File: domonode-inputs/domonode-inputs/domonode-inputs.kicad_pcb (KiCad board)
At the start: 2 copper layers, 95 x 80 mm, 66 parts, among them P1 CONN_01X02, P10 CONN_01X02, P11 CONN_01X02, P12 CONN_02X03, P13 CONN_02X05, P14 CONN_01X06, P2 CONN_01X02, P3 CONN_01X02, P4 CONN_01X02, P5 CONN_01X02, P6 CONN_01X02, P7 CONN_01X02, P8 CONN_01X02, P9 CONN_01X02, U1 TLP620, U10 TLP620, U11 PCA9555, U12 24LC02, U13 TLP620, U2 TLP620, U3 TLP620, U4 TLP620, U5 TLP620, U6 TLP620, U7 TLP620, U8 TLP620, U9 TLP620

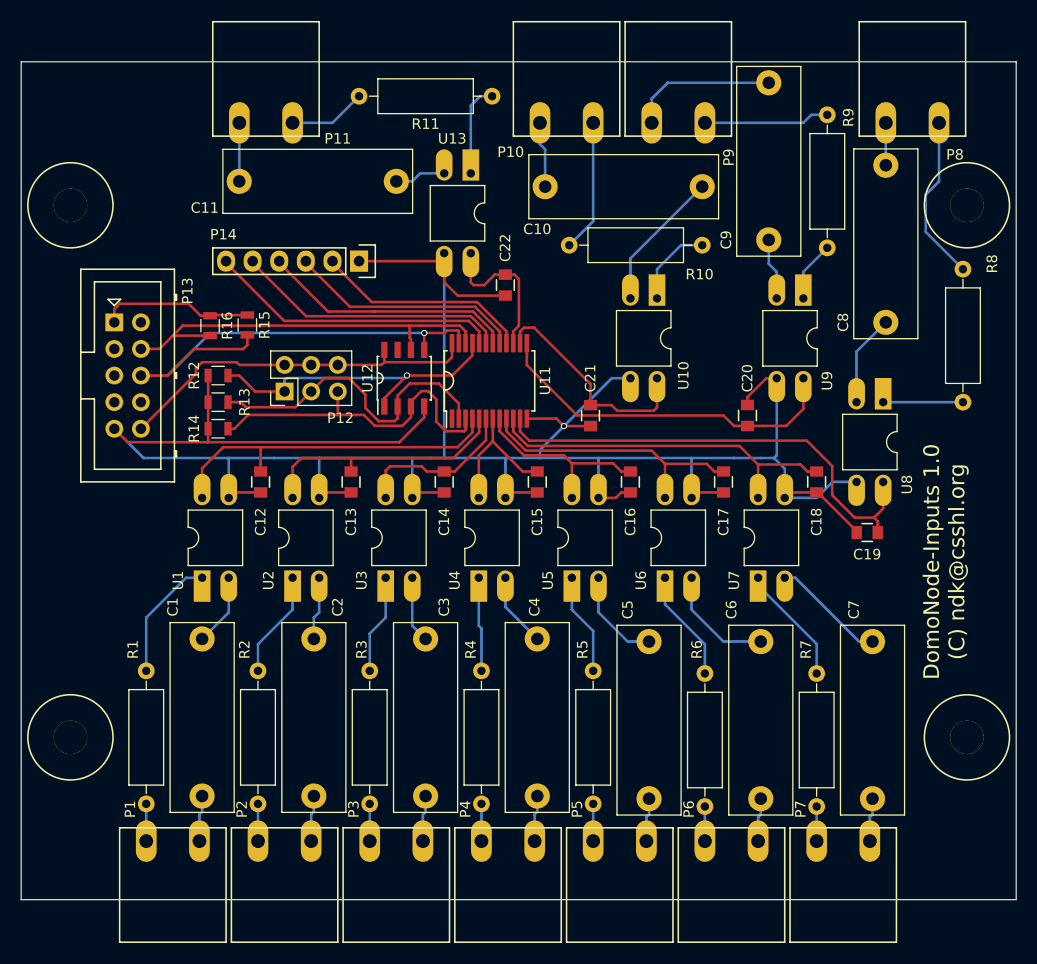
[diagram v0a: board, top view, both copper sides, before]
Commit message: Updated DomoNode-Inputs design files: - added component values in schematic (w/ minor changes for readability) - changed X2 capacitors footprint - moved filter capacitors to a regular pattern, where possible - slightly changed layout to account for new footprints
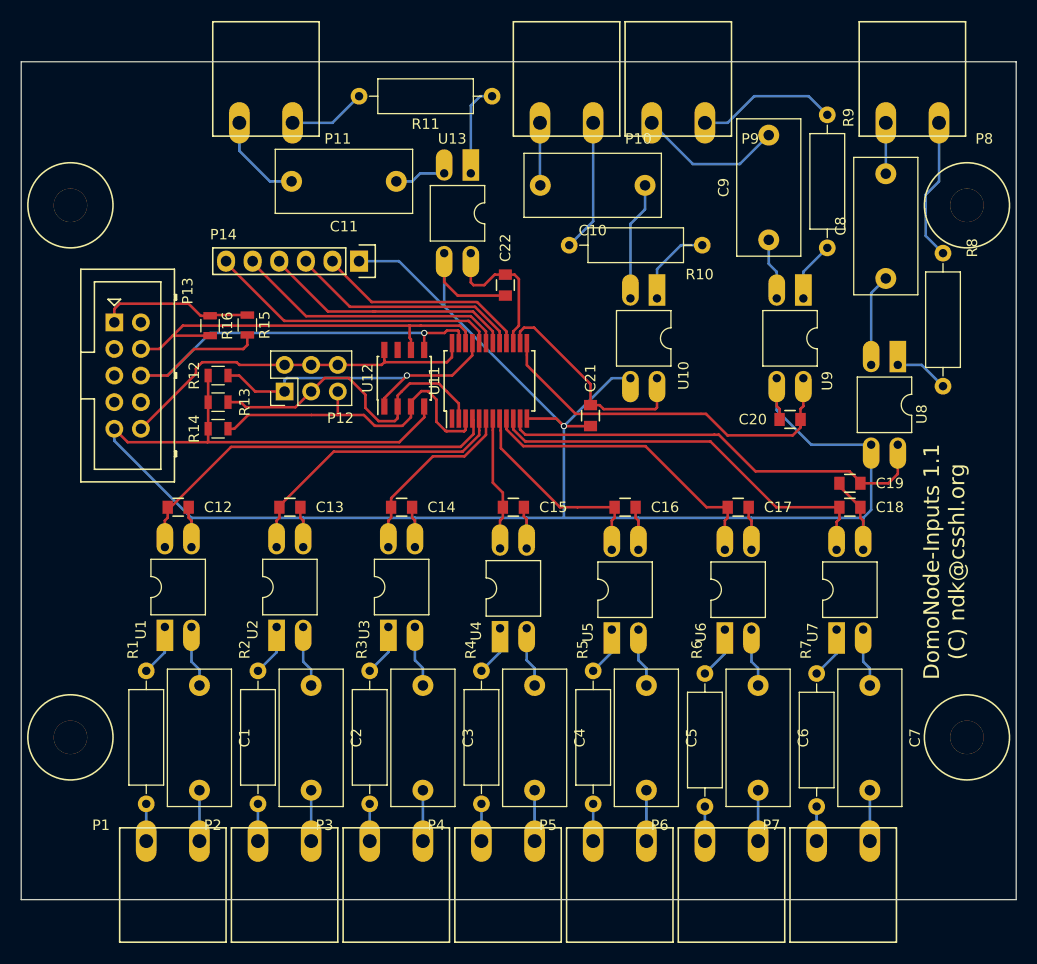
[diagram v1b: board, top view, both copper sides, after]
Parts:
- C1, C10, C11, C2, C3, C4, C5, C6, C7, C8, C9: value C -> 100uF X2; footprint Capacitors_ThroughHole:C_Rect_L18.0mm_W6.0mm_P15.00mm_FKS3_FKP3 -> Capacitors_ThroughHole:C_Rect_L13.0mm_W6.0mm_P10.00mm_FKS3_FKP3_MKS4
- C12, C13, C14, C15, C16, C17, C18, C19, C20, C21, C22: value C -> 1uF
- R1, R10, R11, R2, R3, R4, R5, R6, R7, R8, R9: value R -> 1k 1/4W
- R12, R13, R14, R15, R16: value R -> 10k
- U11: footprint AAA mie lib verificate:SSOP-24_5.3x8.2mm_Pitch0.65mm -> Housings_SSOP:SSOP-24_5.3x8.2mm_Pitch0.65mm
- U12: footprint AAA mie lib verificate:SOIC-8_3.9x4.9mm_Pitch1.27mm -> Housings_SOIC:SOIC-8_3.9x4.9mm_Pitch1.27mm
- moved U7 8.98 mm to (218.1, 80.6)
- moved C12 8.24 mm to (155.2, 69.0), turned to 0 degrees
- moved U6 7.56 mm to (207.4, 80.6)
- moved C13 6.32 mm to (165.9, 69.0), turned to 0 degrees
- moved U5 6.25 mm to (196.6, 80.6)
- moved U1 5.89 mm to (153.9, 80.4)
- moved C10 5.46 mm to (199.8, 38.2)
- moved U4 5.24 mm to (185.9, 80.5)
- moved C19 4.98 mm to (219.3, 66.7)
- moved U2 4.94 mm to (164.6, 80.4)
- moved C14 4.73 mm to (176.5, 69.0), turned to 0 degrees
- moved U3 4.71 mm to (175.3, 80.4)
- moved C4 4.45 mm to (189.2, 86.0)
- moved C1 4.45 mm to (157.2, 86.0)
- moved C2 4.45 mm to (167.9, 86.0)
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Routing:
- net GND: track 234.4 -> 254.6 mm
- net Net-(R1-Pad1): track 12.0 -> 4.93 mm
- net Net-(R7-Pad1): track 11.5 -> 4.98 mm
- net Net-(R6-Pad1): track 10.7 -> 4.98 mm
- net Net-(R2-Pad1): track 10.3 -> 4.93 mm
- net Net-(C6-Pad1): track 10.9 -> 5.60 mm
- net Net-(C7-Pad1): track 10.9 -> 5.60 mm
- net Net-(R5-Pad1): track 9.73 -> 4.67 mm
- net /IN8: track 47.4 -> 42.5 mm
- net Net-(R3-Pad1): track 9.52 -> 4.93 mm
- net /IN7: track 35.0 -> 39.4 mm
- net Net-(R4-Pad1): track 9.00 -> 4.80 mm
- net /IN1: track 33.7 -> 37.4 mm
- net Net-(C5-Pad1): track 9.29 -> 5.65 mm
- net Net-(C11-Pad2): track 5.59 -> 8.86 mm
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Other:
- board text added: "DomoNode-Inputs 1.1 (C) ndk@csshl.org"
- board text removed: "DomoNode-Inputs 1.0 (C) ndk@csshl.org"
